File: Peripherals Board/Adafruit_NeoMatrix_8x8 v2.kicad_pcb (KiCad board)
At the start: 2 copper layers, 71.1 x 71.1 mm, 155 parts

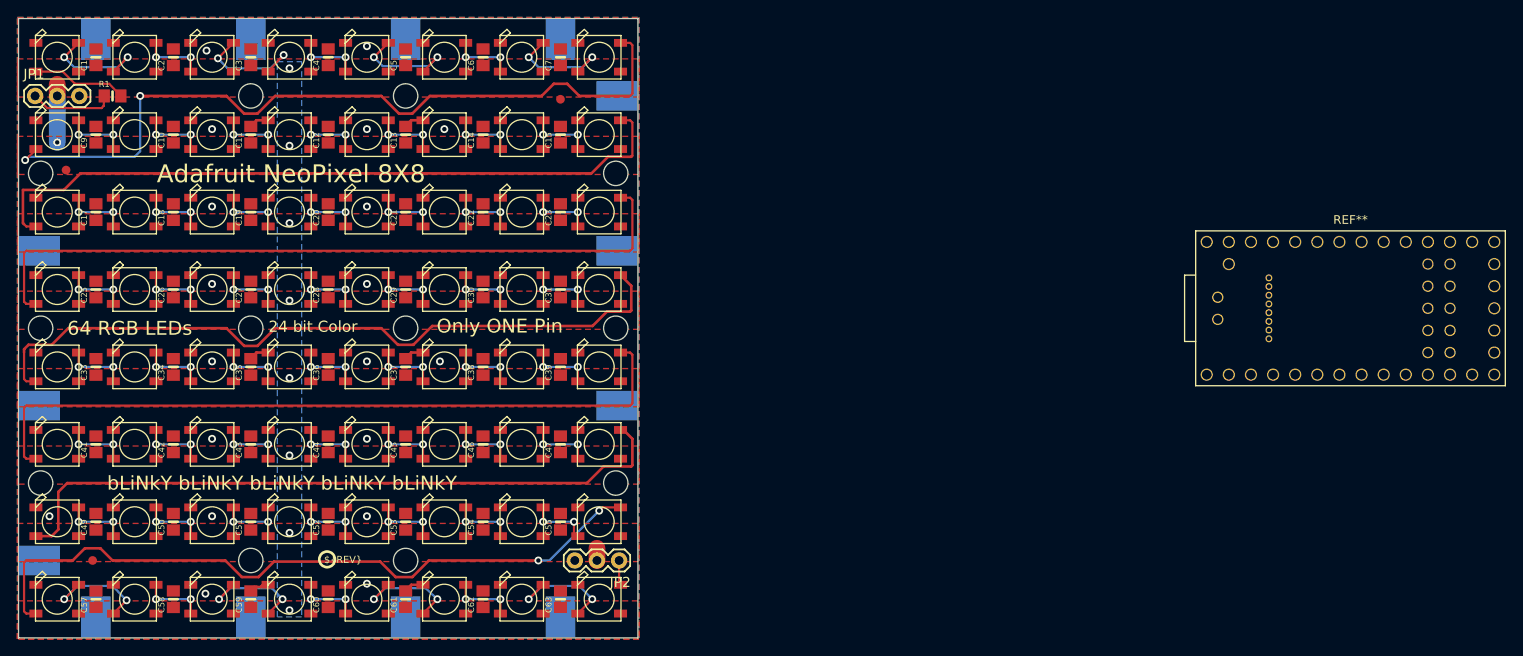
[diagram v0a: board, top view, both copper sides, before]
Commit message: Add footprints and layouts
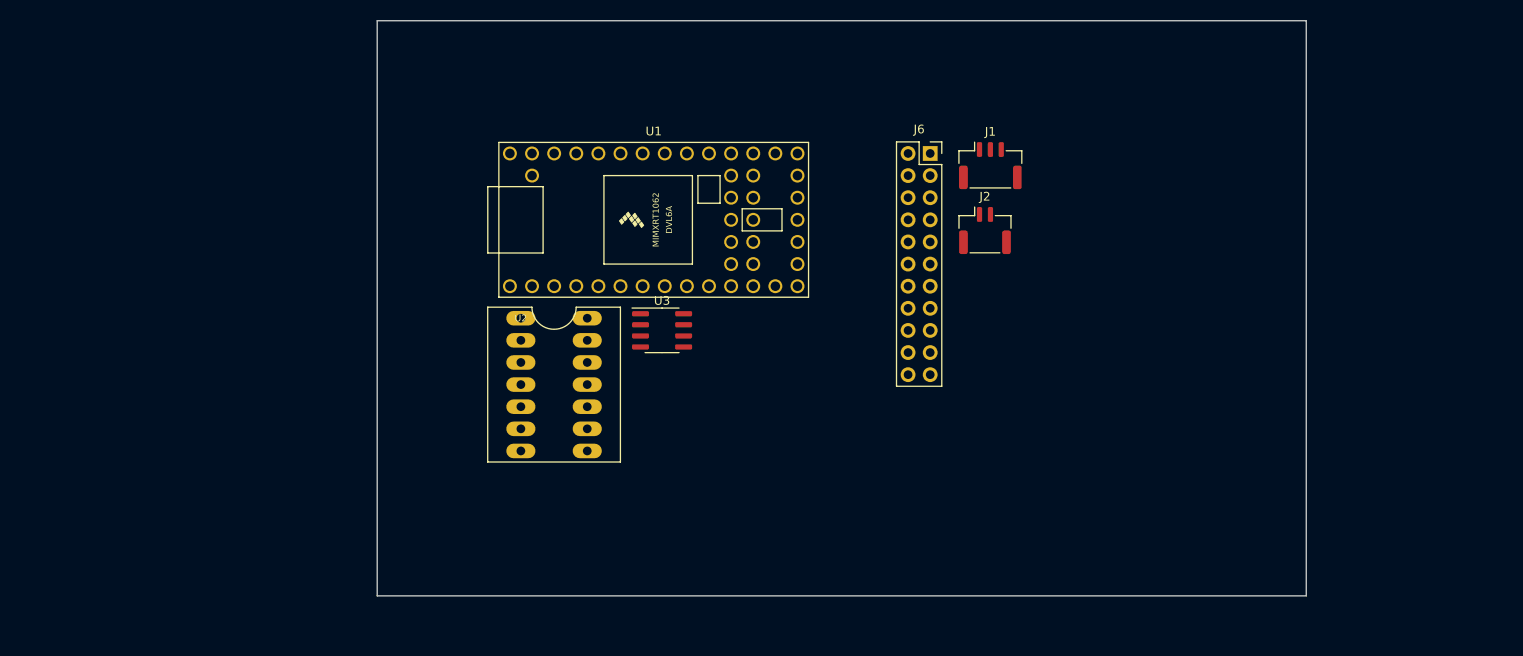
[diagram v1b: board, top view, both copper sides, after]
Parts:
- removed @HOLE0, @HOLE1, @HOLE10, @HOLE11, @HOLE2, @HOLE3, @HOLE4, @HOLE5, @HOLE6, @HOLE7, @HOLE8, @HOLE9: , 
- removed C1, C10, C11, C12, C13, C14, C15, C17, C18, C19, C2, C20, C21, C22, C23, C25, C26, C27, C28, C29, C3, C30, C31, C33, C34, C35, C36, C37, C38, C39, C4, C41, C42, C43, C44, C45, C46, C47, C49, C5, C50, C51, C52, C53, C54, C55, C57, C58, C59, C6, C60, C61, C62, C63, C7, C9, R1: , Adafruit_NeoMatrix_8x8 v2:0805-NO
- removed FID1, FID2, FID3: FIDUCIAL"", Adafruit_NeoMatrix_8x8 v2:FIDUCIAL_1MM
- removed JP1, JP2: , Adafruit_NeoMatrix_8x8 v2:1X03
- removed LED1, LED10, LED11, LED12, LED13, LED14, LED15, LED16, LED17, LED18, LED19, LED2, LED20, LED21, LED22, LED23, LED24, LED25, LED26, LED27, LED28, LED29, LED3, LED30, LED31, LED32, LED33, LED34, LED35, LED36, LED37, LED38, LED39, LED4, LED40, LED41, LED42, LED43, LED44, LED45, LED46, LED47, LED48, LED49, LED5, LED50, LED51, LED52, LED53, LED54, LED55, LED56, LED57, LED58, LED59, LED6, LED60, LED61, LED62, LED63, LED64, LED7, LED8, LED9: WS2812B5050, Adafruit_NeoMatrix_8x8 v2:WS2812B
- removed REF**: Teensy 4.0, teensy:Teensy40_SMT
- removed TP1, TP10, TP11, TP12, TP13, TP14, TP2, TP3, TP4, TP5, TP6, TP7, TP8, TP9: , Adafruit_NeoMatrix_8x8 v2:TESTPOINT_SMT
- removed U$1: , Adafruit_NeoMatrix_8x8 v2:ADAFRUIT_TEXT_30MM
- removed U$2: , Adafruit_NeoMatrix_8x8 v2:PCBFEAT-REV-040
- added J1: Conn_01x03_Pin, Connector_JST:JST_GH_SM03B-GHS-TB_1x03-1MP_P1.25mm_Horizontal, F.Cu at (159.3, 82.7)
- added J2: Conn_01x02_Pin, Connector_JST:JST_GH_SM02B-GHS-TB_1x02-1MP_P1.25mm_Horizontal, F.Cu at (158.7, 90.1)
- added J6: Conn_02x11_Counter_Clockwise, Connector_PinSocket_2.54mm:PinSocket_2x11_P2.54mm_Vertical, F.Cu at (152.4, 81.3)
- added U1: Teensy4.0, teensy:Teensy40, F.Cu at (120.7, 88.9)
- added U2: 74AHC125, 74AHC125:14DIP, F.Cu at (105.4, 100.2)
- added U3: SN65HVD230, Package_SO:SOIC-8_3.9x4.9mm_P1.27mm, F.Cu at (121.6, 101.6)
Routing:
- net N$2: track 90.0 -> 0.00 mm, vias 2 -> 0
- net N$6: track 84.3 -> 0.00 mm
- net N$5: track 84.2 -> 0.00 mm
- net N$4: track 84.2 -> 0.00 mm
- net N$8: track 82.4 -> 0.00 mm, vias 2 -> 0
- net N$3: track 82.3 -> 0.00 mm
- net N$7: track 79.2 -> 0.00 mm
- net GND: track 13.8 -> 0.00 mm, vias 19 -> 0
- net N$37: track 13.8 -> 0.00 mm, vias 2 -> 0
- net N$118: track 13.2 -> 0.00 mm, vias 2 -> 0
- net N$114: track 13.0 -> 0.00 mm, vias 2 -> 0
- net N$116: track 13.0 -> 0.00 mm, vias 2 -> 0
- net N$94: track 13.0 -> 0.00 mm, vias 2 -> 0
- net N$59: track 12.9 -> 0.00 mm, vias 2 -> 0
- net N$41: track 12.9 -> 0.00 mm, vias 2 -> 0
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- removed copper zone on B.Cu, net GND
- removed copper zone on F.Cu, net GND
- removed copper zone on B.Cu, net VDD
- removed copper zone on F.Cu, net VDD
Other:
- board size 71.1 x 71.1 mm -> 106.7 x 66 mm
- board text removed: "24 bit Color"
- board text removed: "5V"
- board text removed: "64 RGB LEDs"
- board text removed: "Adafruit NeoPixel 8X8"
- board text removed: "DIN"
- board text removed: "DOUT"
- board text removed: "GND"
- board text removed: "Only ONE Pin"
- board text removed: "bLiNkY bLiNkY bLiNkY bLiNkY bLiNkY"
